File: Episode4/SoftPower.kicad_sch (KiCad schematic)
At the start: 48 parts, among them J10 ATX POWER, SW1 POWER, U1 74HCT14, U2 74HCT74

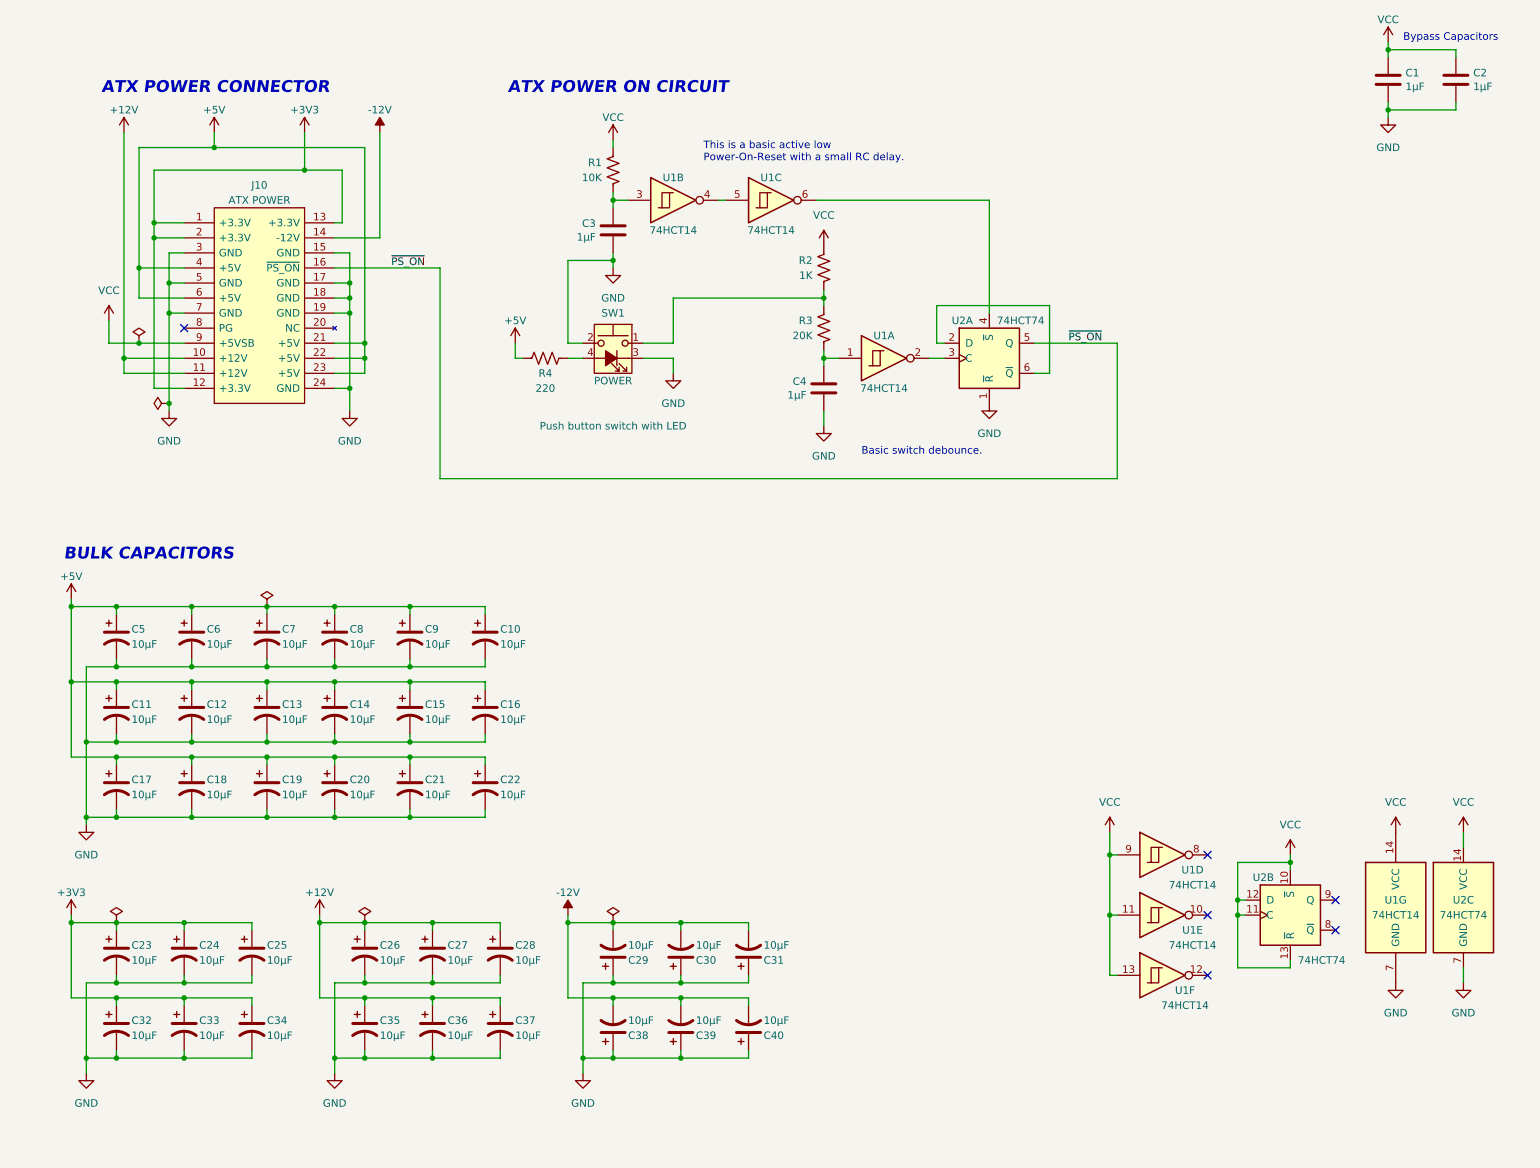
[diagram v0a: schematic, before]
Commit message: Added more capacitors and extended the bus form 7 to 12
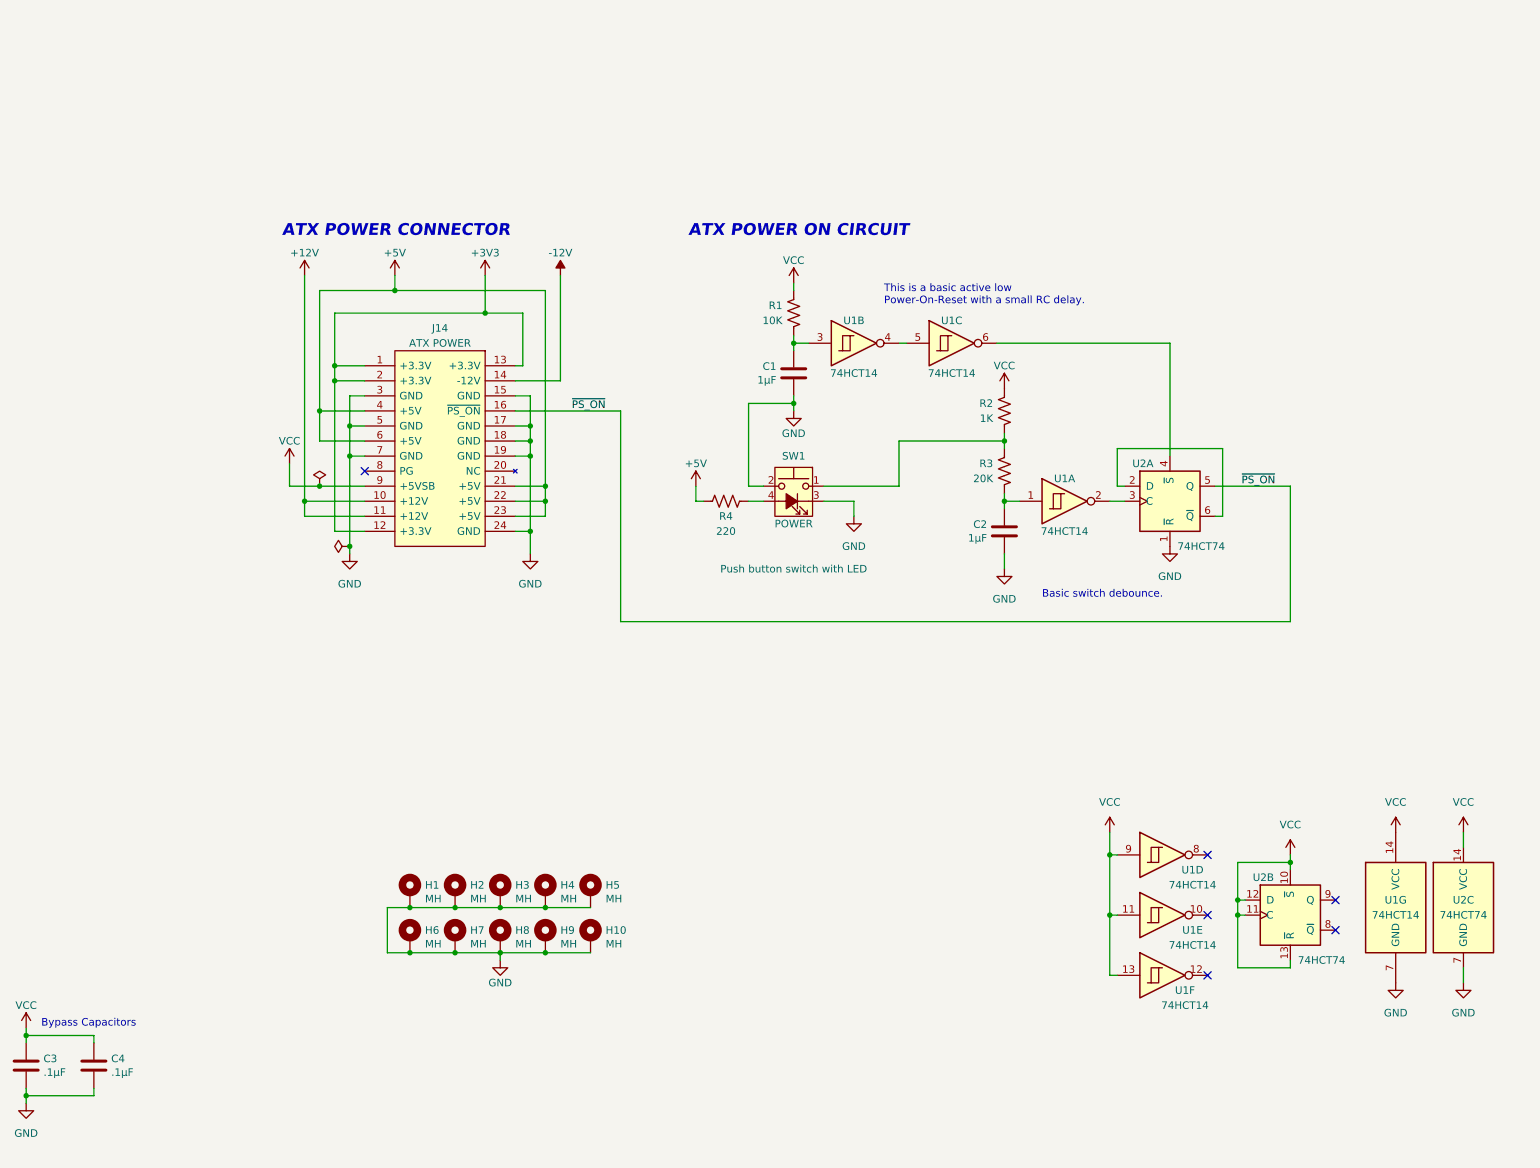
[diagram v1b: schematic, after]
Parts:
- removed C10, C11, C12, C13, C14, C15, C16, C17, C18, C19, C20, C21, C22, C23, C24, C25, C26, C27, C28, C29, C30, C31, C32, C33, C34, C35, C36, C37, C38, C39, C40, C5, C6, C7, C8, C9: 10µF, Capacitor_THT:CP_Radial_D5.0mm_P2.50mm, symbol Device:C_Polarized_US
- added H1, H10, H2, H3, H4, H5, H6, H7, H8, H9: MH, MountingHole:MountingHole_3.5mm_Pad_Via, symbol Mechanical:MountingHole_Pad
- C1: renamed from C3; footprint Capacitor_THT:C_Disc_D3.0mm_W1.6mm_P2.50mm -> Capacitor_THT:C_Disc_D3.4mm_W2.1mm_P2.50mm
- C2: renamed from C4; footprint Capacitor_THT:C_Disc_D3.0mm_W1.6mm_P2.50mm -> Capacitor_THT:C_Disc_D3.4mm_W2.1mm_P2.50mm
- C3: renamed from C1; value 1µF -> .1µF; footprint Capacitor_THT:C_Disc_D3.0mm_W1.6mm_P2.50mm -> Capacitor_THT:C_Disc_D3.4mm_W2.1mm_P2.50mm
- C4: renamed from C2; value 1µF -> .1µF; footprint Capacitor_THT:C_Disc_D3.0mm_W1.6mm_P2.50mm -> Capacitor_THT:C_Disc_D3.4mm_W2.1mm_P2.50mm
- renumbered J10 to J14
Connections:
- net GND: now also H1.1, H10.1, H2.1, H3.1, H4.1, H5.1, H6.1, H7.1, H8.1, H9.1
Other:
- note removed: "BULK CAPACITORS"
- moved on the sheet: C1, C2, C3, C4, J14, R1, R2, R3, R4, SW1, U1A, U1B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

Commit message: Worked on BOM
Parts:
- added D1, D5: TVS 5V, Diode_SMD:D_SMB, symbol Diode:SM6T6V8A
- added D2, D6: TVS 3V3, Diode_SMD:D_SMB, symbol Diode:SM6T6V8A
- added D3, D4, D7, D8: TVS 12V, Diode_SMD:D_SMB, symbol Diode:SM6T6V8A
- C1, C2: footprint Capacitor_THT:C_Disc_D3.4mm_W2.1mm_P2.50mm -> Capacitor_SMD:C_0805_2012Metric_Pad1.18x1.45mm_HandSolder; Manufacturer_Name (none) -> Samsung Electro-Mechanics; Manufacturer_Part_Number (none) -> CL21B105KBFNNNG
- C3, C4: footprint Capacitor_THT:C_Disc_D3.4mm_W2.1mm_P2.50mm -> Capacitor_SMD:C_0805_2012Metric_Pad1.18x1.45mm_HandSolder; Manufacturer_Name (none) -> Samsung Electro-Mechanics; Manufacturer_Part_Number (none) -> CL21B104KBFNNNG
- H1, H10, H2, H3, H4, H5, H6, H7, H8, H9: now not fitted
- R1: footprint Resistor_THT:R_Axial_DIN0207_L6.3mm_D2.5mm_P10.16mm_Horizontal -> Resistor_SMD:R_0805_2012Metric_Pad1.20x1.40mm_HandSolder; Manufacturer_Name (none) -> Bourns; Manufacturer_Part_Number (none) -> CR0805-FX-1002ELF
- R2: footprint Resistor_THT:R_Axial_DIN0207_L6.3mm_D2.5mm_P10.16mm_Horizontal -> Resistor_SMD:R_0805_2012Metric_Pad1.20x1.40mm_HandSolder; Manufacturer_Name (none) -> Bourns; Manufacturer_Part_Number (none) -> CR0805-FX-1001ELF
- R3: footprint Resistor_THT:R_Axial_DIN0207_L6.3mm_D2.5mm_P10.16mm_Horizontal -> Resistor_SMD:R_0805_2012Metric_Pad1.20x1.40mm_HandSolder; Manufacturer_Name (none) -> Bourns; Manufacturer_Part_Number (none) -> CR0805-FX-2002ELF
- R4: value 220 -> 330; footprint Resistor_THT:R_Axial_DIN0207_L6.3mm_D2.5mm_P10.16mm_Horizontal -> Resistor_SMD:R_0805_2012Metric_Pad1.20x1.40mm_HandSolder; Manufacturer_Name (none) -> Bourns; Manufacturer_Part_Number (none) -> CR0805-FX-3300ELF
- SW1: Manufacturer_Name (none) -> Same Sky; Manufacturer_Part_Number (none) -> TS29-1212-1-G-300-D
- U1: footprint Package_DIP:DIP-14_W7.62mm_Socket_LongPads -> Package_SO:SOIC-14_3.9x8.7mm_P1.27mm; Manufacturer_Name (none) -> Texas Instruments; Manufacturer_Part_Number (none) -> CD74HCT14M96
- U2: footprint Package_DIP:DIP-14_W7.62mm_Socket_LongPads -> Package_SO:SOIC-14_3.9x8.7mm_P1.27mm; Manufacturer_Name (none) -> Texas Instruments; Manufacturer_Part_Number (none) -> CD74HCT74M96
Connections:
- net +12V: now also D3.1 (A1), D7.1 (A1)
- net +3V3: now also D2.1 (A1), D6.1 (A1)
- net +5V: now also D1.1 (A1), D5.1 (A1)
- net -12V: now also D4.2 (A2), D8.2 (A2)
- net GND: now also D1.2 (A2), D2.2 (A2), D3.2 (A2), D4.1 (A1), D5.2 (A2), D6.2 (A2), D7.2 (A2), D8.1 (A1)
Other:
- note added: "ESD Protection (At ATX PSU connector level)"
- note added: "ESD Protection (At header pin connector level)"
- moved on the sheet: C1, C2, J14, R1, R2, R3, R4, SW1, U1A, U1B, U1C, U2A

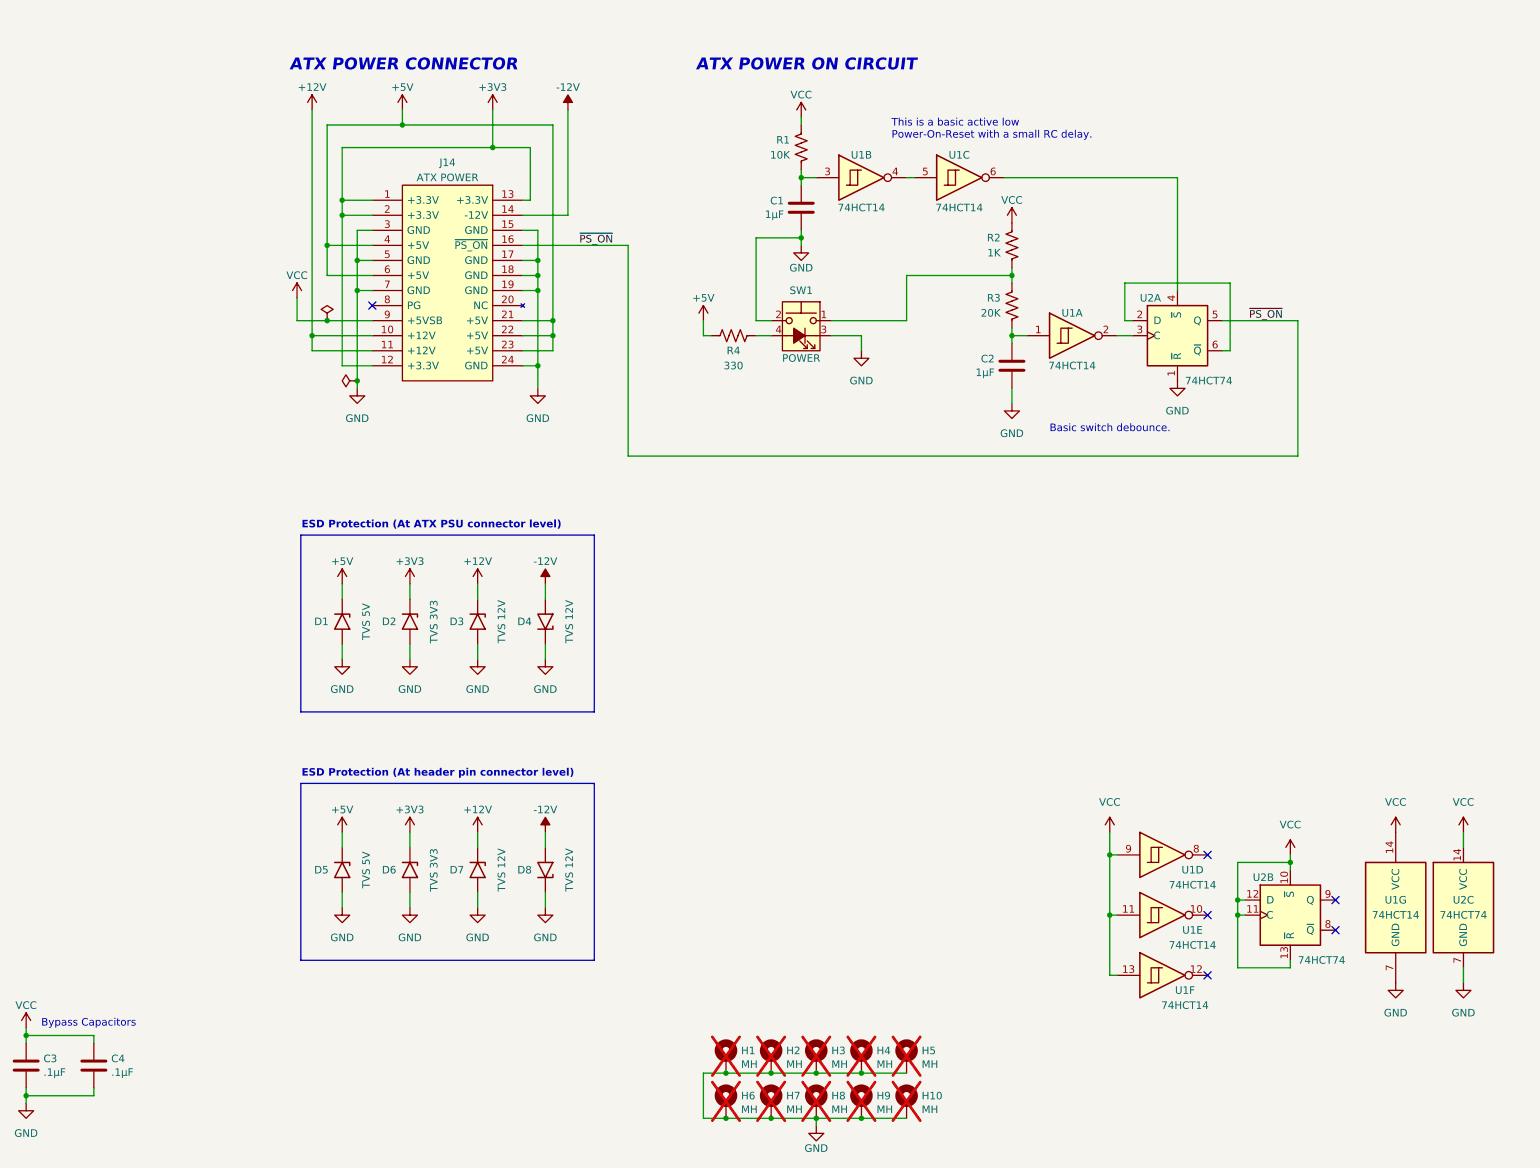
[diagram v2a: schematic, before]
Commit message: Changed bus from 62 to 72 pins
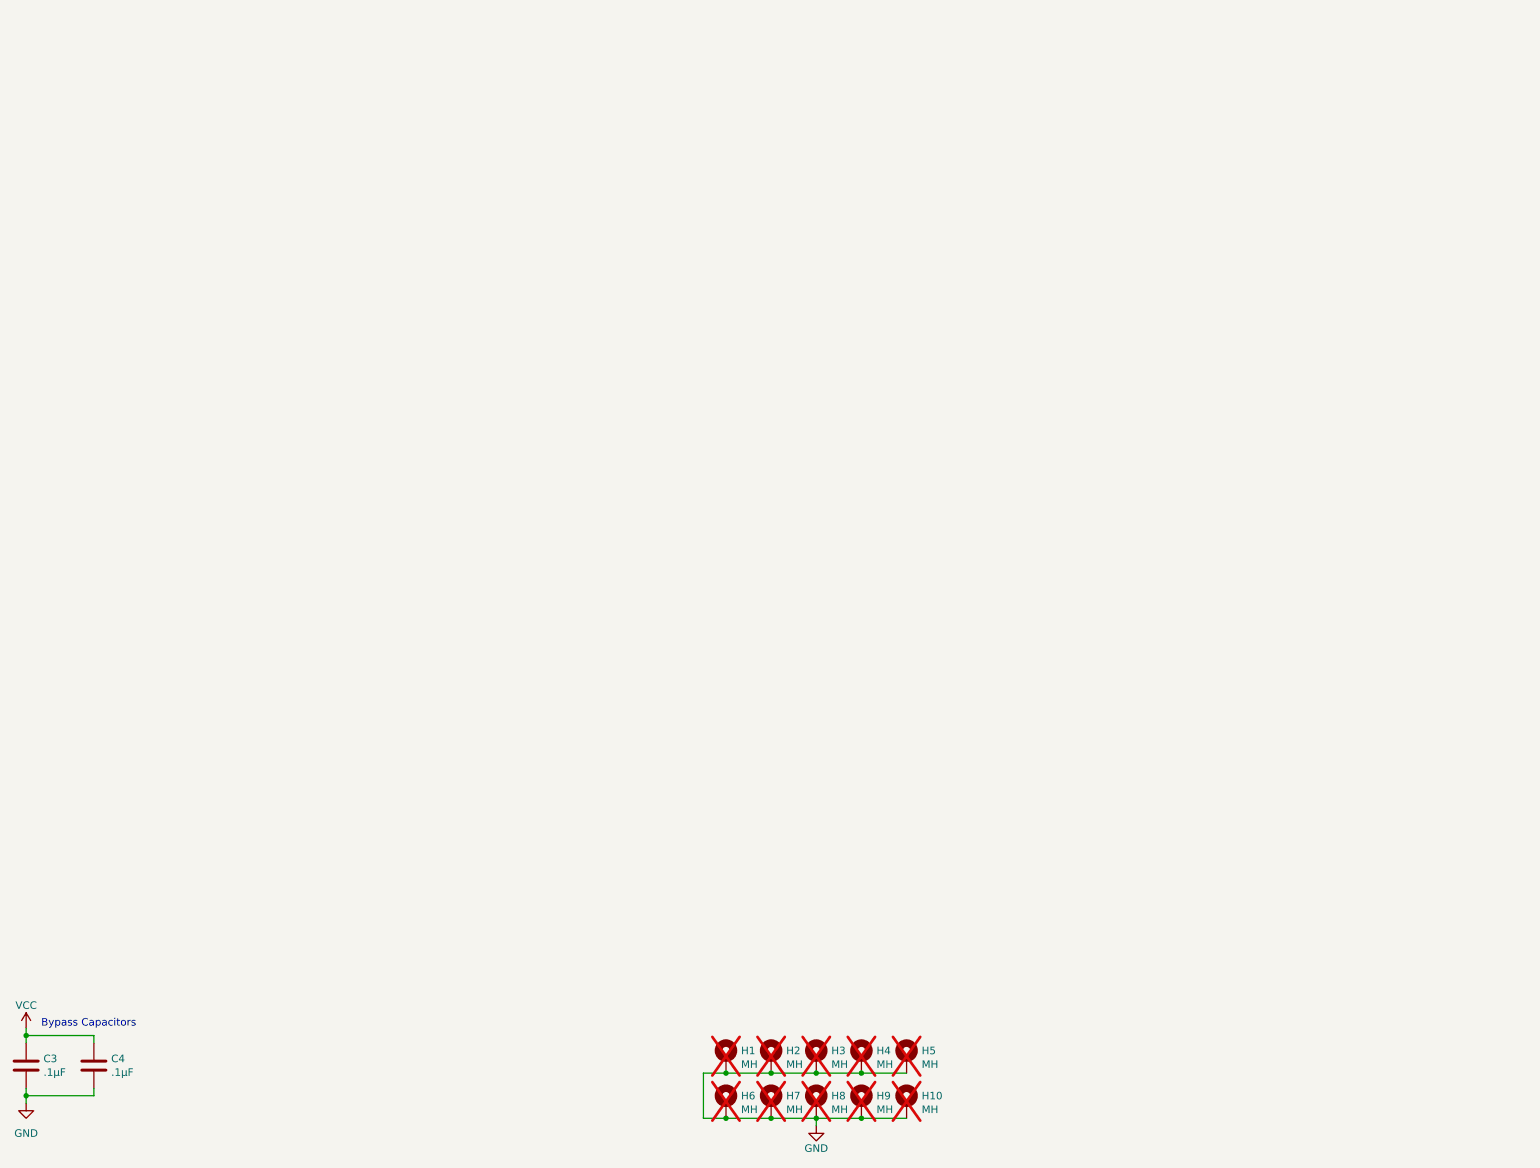
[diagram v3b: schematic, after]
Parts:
- removed C1, C2: 1µF, Capacitor_SMD:C_0805_2012Metric_Pad1.18x1.45mm_HandSolder, symbol Device:C
- removed D1, D5: TVS 5V, Diode_SMD:D_SMB, symbol Diode:SM6T6V8A
- removed D2, D6: TVS 3V3, Diode_SMD:D_SMB, symbol Diode:SM6T6V8A
- removed D3, D4, D7, D8: TVS 12V, Diode_SMD:D_SMB, symbol Diode:SM6T6V8A
- removed J14: ATX POWER, MicroHobbyist:ATX_PSU_CONN, symbol 0_Library:ATX_PSU_CONN
- removed R1: 10K, Resistor_SMD:R_0805_2012Metric_Pad1.20x1.40mm_HandSolder, symbol Device:R_US
- removed R2: 1K, Resistor_SMD:R_0805_2012Metric_Pad1.20x1.40mm_HandSolder, symbol Device:R_US
- removed R3: 20K, Resistor_SMD:R_0805_2012Metric_Pad1.20x1.40mm_HandSolder, symbol Device:R_US
- removed R4: 330, Resistor_SMD:R_0805_2012Metric_Pad1.20x1.40mm_HandSolder, symbol Device:R_US
- removed SW1: POWER, MicroHobbyist:Pushbutton_12mm_LED, symbol Switch:SW_Push_LED
- removed U1: 74HCT14, Package_SO:SOIC-14_3.9x8.7mm_P1.27mm, symbol 74xx:74HC14
- removed U2: 74HCT74, Package_SO:SOIC-14_3.9x8.7mm_P1.27mm, symbol 74xx:74HC74
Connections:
- no-connect marks 6 -> 0
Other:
- note removed: "ATX POWER CONNECTOR"
- note removed: "ATX POWER ON CIRCUIT"
- note removed: "Basic switch debounce."
- note removed: "ESD Protection (At ATX PSU connector level)"
- note removed: "ESD Protection (At header pin connector level)"
- note removed: "This is a basic active low Power-On-Reset with a small RC delay."
